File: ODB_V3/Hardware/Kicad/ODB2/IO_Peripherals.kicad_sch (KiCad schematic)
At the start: 33 parts, among them J1 142-0701-801, J10 MEM2067, J2 GT17HN-4DP-2HA56, J3 GT17HN-4DP-2HA56, J4 USB_B_Micro, J5 SYS_SW_Conn_01x06_Header, J7 Conn_02x04_Odd_Even, Q1 MMBT3904, U1 HM11, U16 USBLC6-2P6, U2 L76L-M33, U9 W25Q512JVEIQ

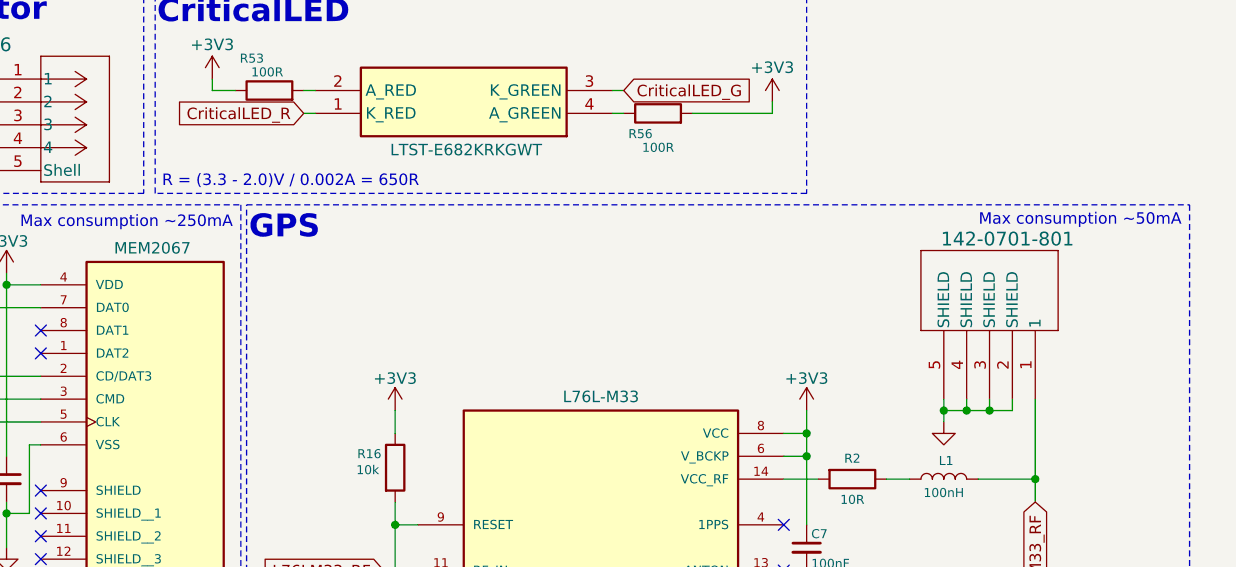
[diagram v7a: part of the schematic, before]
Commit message: wip: fixe library sma + cleanup + trace width
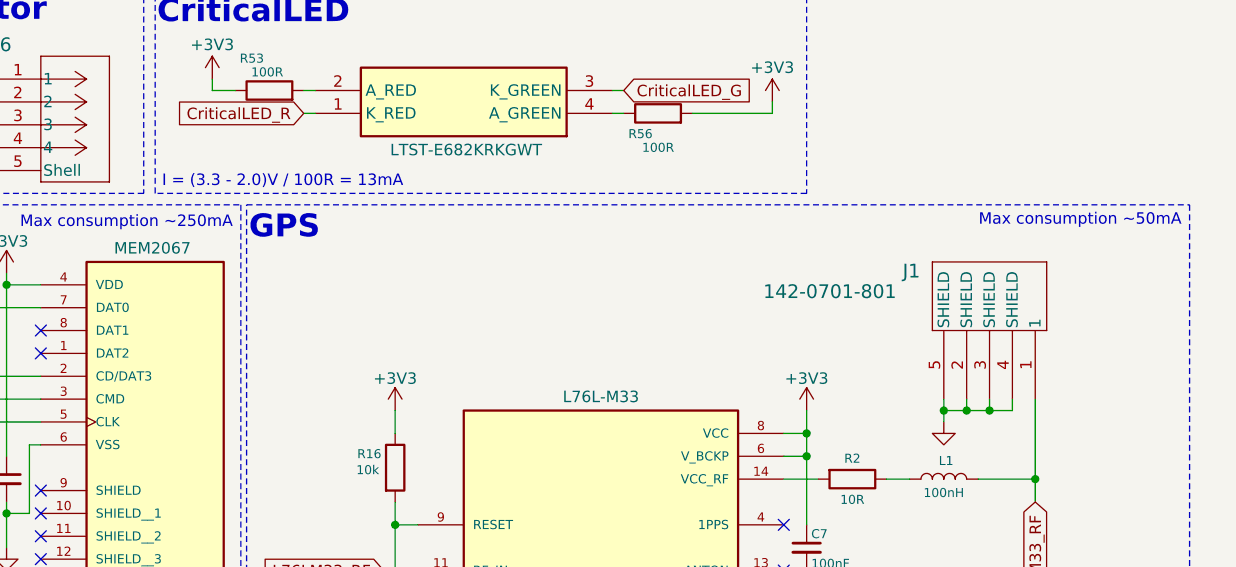
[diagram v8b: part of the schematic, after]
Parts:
- removed J1: 142-0701-801, ODB:CONN_142-0701-801, symbol L76LM33_Library:142-0701-801
- added J1: 142-0701-801, CONN_142-0701-801, symbol ODB2:142-0701-801
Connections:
- net GND: now also J1.2 (SHIELD), J1.3 (SHIELD), J1.4 (SHIELD), J1.5 (SHIELD)
- net L76LM33_RF: now also J1.1
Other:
- note added: "I = (3.3 - 2.0)V / 100R = 13mA"
- note removed: "R = (3.3 - 2.0)V / 0.002A = 650R"
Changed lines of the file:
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@@
 		)
 	)
-	(text "R = (3.3 - 2.0)V / 0.002A = 650R"
+	(text "I = (3.3 - 2.0)V / 100R = 13mA"
 		(exclude_from_sim no)
 		(at 60.452 107.95 0)
@@
 	)
 	(symbol
+		(lib_id "ODB2:142-0701-801")
+		(at 147.32 132.08 90)
+		(unit 1)
+		(exclude_from_sim no)
+		(in_bom yes)
+		(on_board yes)
+		(dnp no)
+		(property "Reference" "J1"
+			(at 142.748 117.856 90)
+			(effects
+				(font
+					(size 1.524 1.524)
+				)
+				(justify right)
+			)
+		)
+		(property "Value" "142-0701-801"
+			(at 127.254 120.142 90)
+			(effects
+				(font
+					(size 1.524 1.524)
+				)
+				(justify right)
+			)
+		)
+		(property "Footprint" "CONN_142-0701-801"
+			(at 147.32 132.08 0)
+			(effects
+				(font
+					(size 1.27 1.27)
+					(italic yes)
+				)
+				(hide yes)
+			)
+		)
+		(property "Datasheet" "142-0701-801"
+			(at 147.32 132.08 0)
+			(effects
+				(font
+					(size 1.27 1.27)
+					(italic yes)
+				)
+				(hide yes)
+			)
+		)
+		(property "Description" ""
+			(at 147.32 132.08 0)
+			(effects
+				(font
+					(size 1.27 1.27)
+				)
+				(hide yes)
+			)
+		)
+		(pin "5"
+		)
+		(pin "4"
+		)
+		(pin "2"
+		)
+		(pin "3"
+		)
+		(pin "1"
+		)
+		(instances
+			(project ""
+				(path "/4b06c5d1-aa8b-48ed-8972-b43a60cfab78/93865dc8-71fa-4dc6-90ce-f5a9779dfd41"
+					(reference "J1")
+					(unit 1)
+				)
+			)
+		)
+	)
+	(symbol
 		(lib_id "power:+3V3")
 		(at 128.27 99.06 0)
@@
 					(unit 1)
 				)
-			)
-		)
-	)
-	(symbol
-		(lib_id "L76LM33_Library:142-0701-801")
-		(at 157.48 132.08 270)
-		(mirror x)
-		(unit 1)
-		(exclude_from_sim no)
-		(in_bom yes)
-		(on_board yes)
-		(dnp no)
-		(property "Reference" "J1"
-			(at 153.67 112.014 90)
-			(effects
-				(font
-					(size 1.524 1.524)
-				)
-				(justify right)
-				(hide yes)
-			)
-		)
-		(property "Value" "142-0701-801"
-			(at 161.798 114.3 90)
-			(effects
-				(font
-					(size 1.524 1.524)
-				)
-				(justify right)
-			)
-		)
-		(property "Footprint" "ODB:CONN_142-0701-801"
-			(at 157.48 132.08 0)
-			(effects
-				(font
-					(size 1.27 1.27)
-					(italic yes)
-				)
-				(hide yes)
-			)
-		)
-		(property "Datasheet" "https://www.digikey.ca/en/products/detail/cinch-connectivity-solutions-johnson/142-0701-801/35280"
-			(at 157.48 132.08 0)
-			(effects
-				(font
-					(size 1.27 1.27)
-					(italic yes)
-				)
-				(hide yes)
-			)
-		)
-		(property "Description" ""
-			(at 157.48 132.08 0)
-			(effects
-				(font
-					(size 1.27 1.27)
-				)
-				(hide yes)
-			)
-		)
-		(property "DigiKey_Part_Number" "J502-ND"
-			(at 157.48 132.08 90)
-			(effects
-				(font
-					(size 1.27 1.27)
-				)
-				(hide yes)
-			)
-		)
-		(property "Purchase-URL" ""
-			(at 157.48 132.08 90)
-			(effects
-				(font
-					(size 1.27 1.27)
-				)
-				(hide yes)
-			)
-		)
-		(property "Sim.Device" ""
-			(at 157.48 132.08 90)
-			(effects
-				(font
-					(size 1.27 1.27)
-				)
-				(hide yes)
-			)
-		)
-		(property "Sim.Pins" ""
-			(at 157.48 132.08 90)
-			(effects
-				(font
-					(size 1.27 1.27)
-				)
-				(hide yes)
-			)
-		)
-		(property "Sim.Type" ""
-			(at 157.48 132.08 90)
-			(effects
-				(font
-					(size 1.27 1.27)
-				)
-				(hide yes)
-			)
-		)
-		(property "Manufacturer_Part_Number" "142-0701-801"
-			(at 157.48 132.08 90)
-			(effects
-				(font
-					(size 1.27 1.27)
-				)
-				(hide yes)
-			)
-		)
-		(pin "3"
-		)
-		(pin "2"
-		)
-		(pin "5"
-		)
-		(pin "1"
-		)
-		(pin "4"
-		)
-		(instances
-			(project "ODB2"
-				(path "/4b06c5d1-aa8b-48ed-8972-b43a60cfab78/93865dc8-71fa-4dc6-90ce-f5a9779dfd41"
-					(reference "J1")
-					(unit 1)
-				)
